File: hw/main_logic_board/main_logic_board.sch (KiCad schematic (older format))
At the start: 3 parts, among them U1 PocketBeagle, U2 BME280, U3 MPU-9250

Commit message: Progress on MLB design
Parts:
- removed U2: BME280, Package_LGA:Bosch_LGA-8_2.5x2.5mm_P0.65mm_ClockwisePinNumbering, symbol Sensor:BME280
- removed U3: MPU-9250, Sensor_Motion:InvenSense_QFN-24_3x3mm_P0.4mm, symbol Sensor_Motion:MPU-9250
- added C1: 47uF, symbol Device:C_Small
- added TP1: TP_5V, TestPoint:TestPoint_Pad_D2.0mm, symbol Connector:TestPoint
- added TP2: TP_3V3, TestPoint:TestPoint_Pad_D2.0mm, symbol Connector:TestPoint
- added TP3: TP_VOUT, TestPoint:TestPoint_Pad_D2.0mm, symbol Connector:TestPoint
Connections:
- net labels added: +3V3, +5V, AIN_1V8, AIN_3V3, GND, GPIO20, GPIO23, GPIO26, GPIO27, I2C_SCL, I2C_SDA, PWM0, PWM1, RC_OUT_2, RC_OUT_3, RC_OUT_4, RC_OUT_5, RC_OUT_6, SPI1_CLK, SPI1_CS0, SPI1_CS1, SPI1_MISO, SPI1_MOSI, SPI1_SCLK, UART0_RX, UART0_TX, UART2_RX, UART2_TX, UART4_RX, UART4_TX
- wire segments 0 -> 53
- no-connect marks 0 -> 25
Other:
- moved on the sheet: U1

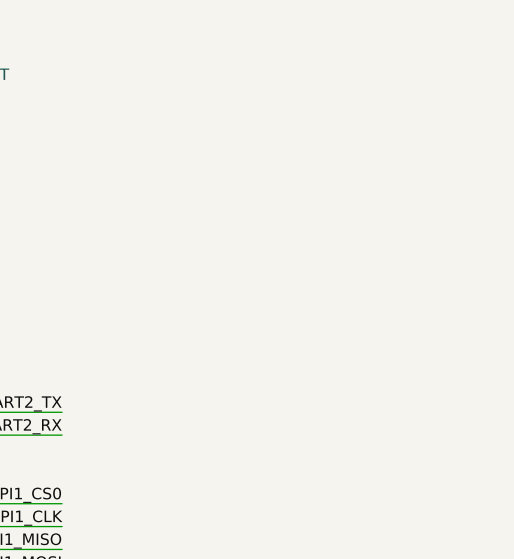
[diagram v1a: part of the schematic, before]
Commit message: Finish initial power schematics, swap some footprints for visualization in pcb view
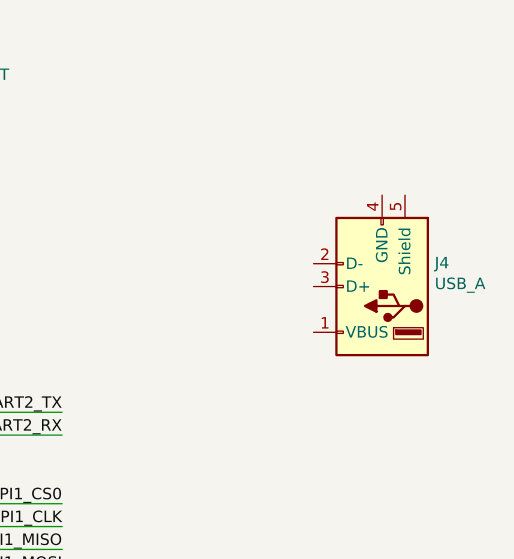
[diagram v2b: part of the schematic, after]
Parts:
- added J4: USB_A, Connector_USB:USB_A_Stewart_SS-52100-001_Horizontal, symbol Connector:USB_A
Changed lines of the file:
@@
 Text Label 5300 4900 0    50   ~ 0
 RC_OUT_6
+$Comp
+L Connector:USB_A J4
+U 1 1 5EAEF3D4
+P 9750 1950
+F 0 "J4" H 9520 1847 50  0000 R CNN
+F 1 "USB_A" H 9520 1938 50  0000 R CNN
+F 2 "Connector_USB:USB_A_Stewart_SS-52100-001_Horizontal" H 9900 1900 50  0001 C CNN
+F 3 " ~" H 9900 1900 50  0001 C CNN
+	1    9750 1950
+	-1   0    0    1
+$EndComp
 $EndSCHEMATC

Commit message: Finish prelim schematic + PCB component placement
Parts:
- added D1, D2, D3, D4: WS2813, LED_SMD:LED_WS2812_PLCC6_5.0x5.0mm_P1.6mm, symbol LED:WS2813
- added H1, H12, H6, H7: GND, MountingHole:MountingHole_2.2mm_M2_Pad_Via, symbol Mechanical:MountingHole_Pad
- added H10, H3, H4, H9: PWR, MountingHole:MountingHole_2.2mm_M2_Pad_Via, symbol Mechanical:MountingHole_Pad
- added H11, H2, H5, H8: SIG, MountingHole:MountingHole_2.2mm_M2_Pad_Via, symbol Mechanical:MountingHole_Pad
- added J10: RC_OUT_6, Connector_PinHeader_1.27mm:PinHeader_1x03_P1.27mm_Vertical, symbol Connector_Generic:Conn_01x03
- added J5: RC_OUT_1, Connector_PinHeader_1.27mm:PinHeader_1x03_P1.27mm_Vertical, symbol Connector_Generic:Conn_01x03
- added J6: RC_OUT_2, Connector_PinHeader_1.27mm:PinHeader_1x03_P1.27mm_Vertical, symbol Connector_Generic:Conn_01x03
- added J7: RC_OUT_3, Connector_PinHeader_1.27mm:PinHeader_1x03_P1.27mm_Vertical, symbol Connector_Generic:Conn_01x03
- added J8: RC_OUT_4, Connector_PinHeader_1.27mm:PinHeader_1x03_P1.27mm_Vertical, symbol Connector_Generic:Conn_01x03
- added J9: RC_OUT_5, Connector_PinHeader_1.27mm:PinHeader_1x03_P1.27mm_Vertical, symbol Connector_Generic:Conn_01x03
- added R5: 0R, Resistor_SMD:R_0805_2012Metric, symbol Device:R_Small_US
- added TP4: AIN_VREF+, TestPoint:TestPoint_Pad_D1.0mm, symbol Connector:TestPoint
- added TP5: AIN_VREF-, TestPoint:TestPoint_Pad_D1.0mm, symbol Connector:TestPoint
- added U9: USBLC6-2P6, lib:SOT50P160X60-6N, symbol USBLC6-2P6:USBLC6-2P6
- C1: footprint (none) -> Capacitor_SMD:C_0805_2012Metric
- TP1: value TP_5V -> TP_5V_VIN; footprint TestPoint:TestPoint_Pad_D2.0mm -> TestPoint:TestPoint_Pad_D1.0mm
- TP2: value TP_3V3 -> TP_3V3_PB; footprint TestPoint:TestPoint_Pad_D2.0mm -> TestPoint:TestPoint_Pad_D1.0mm
- TP3: footprint TestPoint:TestPoint_Pad_D2.0mm -> TestPoint:TestPoint_Pad_D1.0mm
- U1: footprint Module:BeagleBoard_PocketBeagle -> lib:BeagleBoard_PocketBeagle_SMD
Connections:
- net +5V: now also U1.5 (USB1.VBUS), R5.1
- net GND: now also J4.4 (GND), J4.5 (Shield), U1.13 (USB1.ID), H1.1, H12.1, H6.1, H7.1, J10.3 (Pin_3), J5.3 (Pin_3), J6.3 (Pin_3), J7.3 (Pin_3), J8.3 (Pin_3), J9.3 (Pin_3), U9.2 (GND)
- net RC_OUT_2: now also H5.1, J6.2 (Pin_2)
- net RC_OUT_3: now also H8.1, J7.2 (Pin_2)
- net RC_OUT_4: now also H11.1, J8.2 (Pin_2)
- net RC_OUT_5: now also J9.2 (Pin_2)
- net RC_OUT_6: now also J10.2 (Pin_2)
- net at U1.11 (USB1.D+): now also U9.3 (I/O2_1)
- net at U1.17 (AIN.VREF-): now also TP5.1
- net at U1.18 (AIN.VREF+): now also TP4.1
- net AIN_1V8_1: now reaches U1.21 (AIN1(1.8V))
- net RC_OUT_1: now reaches U1.29 (PRU0.7)
- net RC_OUT_1: now also H2.1, J5.2 (Pin_2)
- net I2C1_SCL: now reaches U1.45 (I2C1.SCL)
- net I2C1_SDA: now reaches U1.47 (I2C1.SDA)
- net at U1.9 (USB1.D-): now also U9.1 (I/O1_1)
- net at J4.1 (VBUS): now also R5.2, U9.5 (VBUS)
- net at J4.2 (D-): now also U9.6 (I/O1_2)
- net at J4.3 (D+): now also U9.4 (I/O2_2)
- net +3V3 renamed 3V3_PB
- net AIN_1V8 renamed AIN_1V8_0
- net I2C_SCL renamed I2C2_SCL
- net I2C_SDA renamed I2C2_SDA
- new net +BATT: H10.1, H3.1, H4.1, H9.1, J10.1 (Pin_1), J5.1 (Pin_1), J6.1 (Pin_1), J7.1 (Pin_1), J8.1 (Pin_1), J9.1 (Pin_1)
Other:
- moved on the sheet: J4, TP3

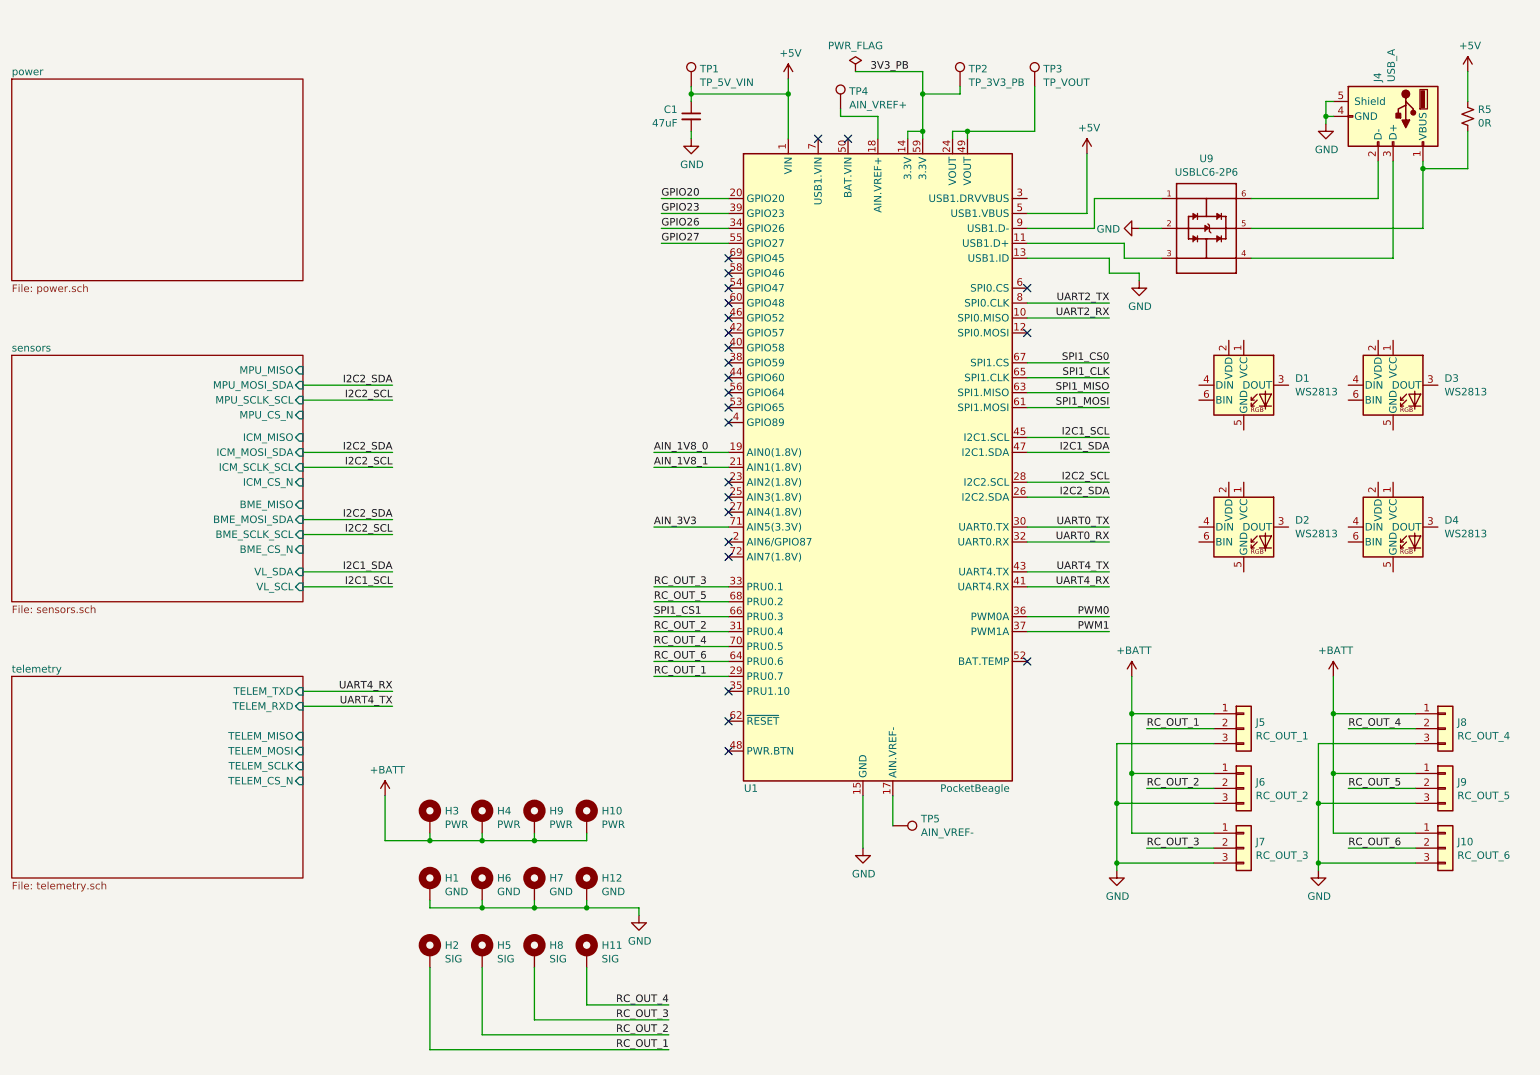
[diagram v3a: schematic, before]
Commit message: Add debug headers, LED wiring, remove MPU
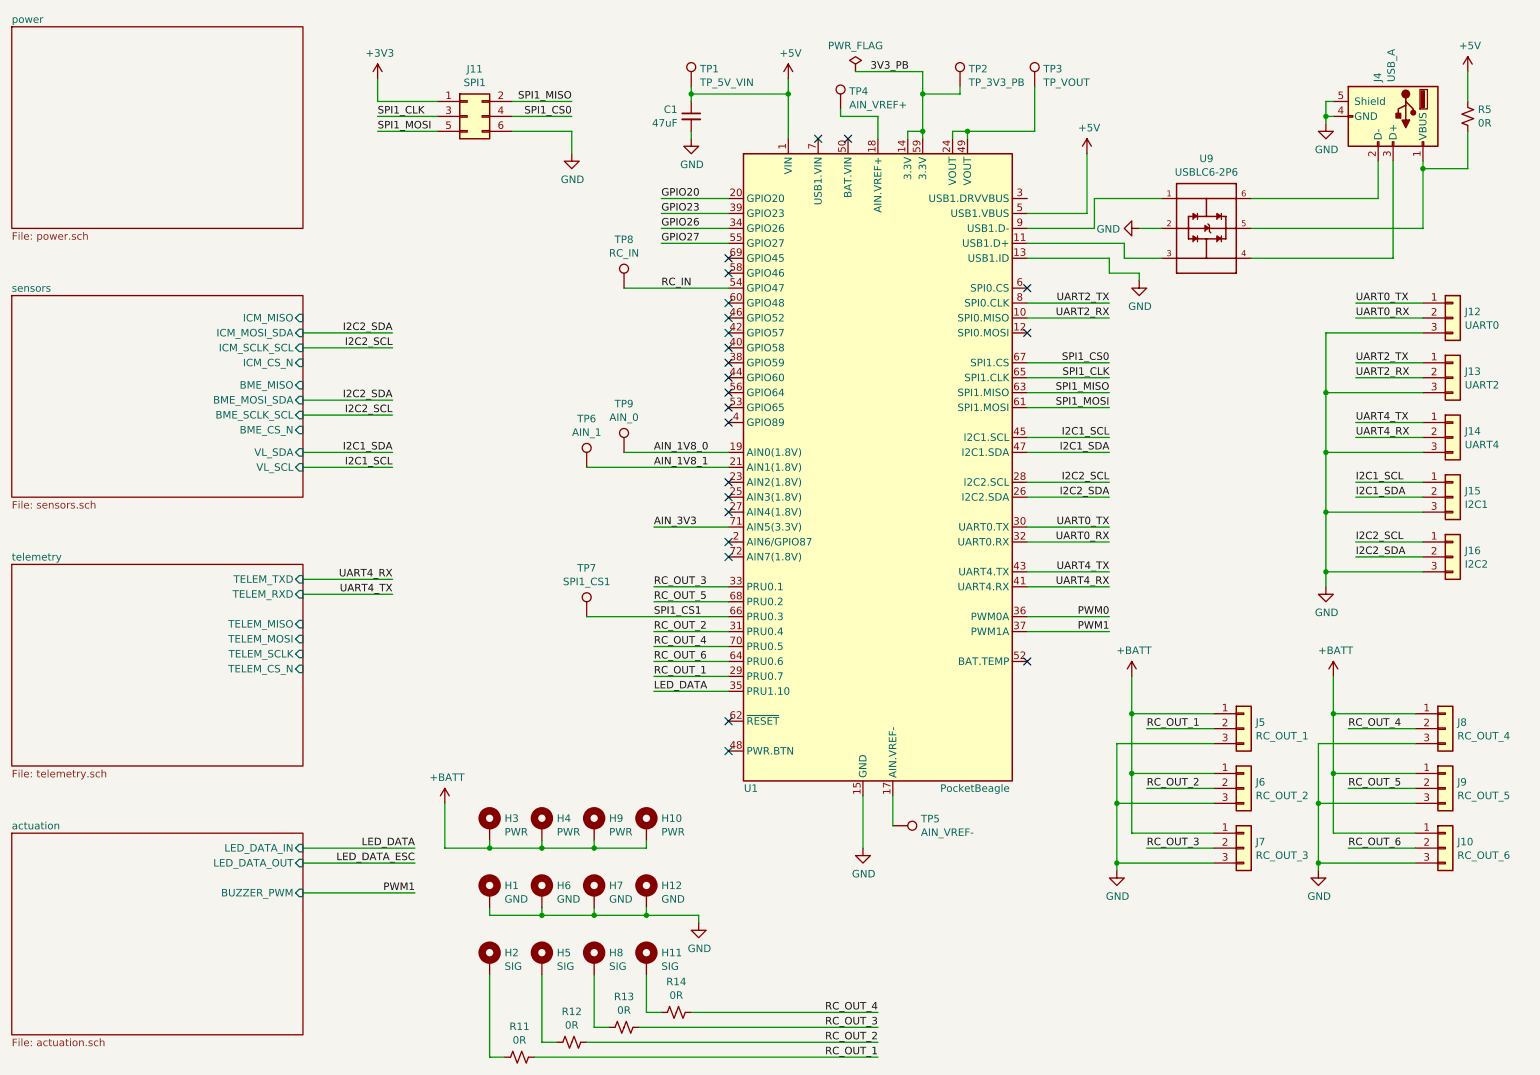
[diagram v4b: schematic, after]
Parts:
- removed D1, D2, D3, D4: WS2813, LED_SMD:LED_WS2812_PLCC6_5.0x5.0mm_P1.6mm, symbol LED:WS2813
- added J11: SPI1, Connector_PinHeader_1.27mm:PinHeader_2x03_P1.27mm_Vertical_SMD, symbol Connector_Generic:Conn_02x03_Odd_Even
- added J12: UART0, Connector_PinHeader_1.27mm:PinHeader_1x03_P1.27mm_Vertical_SMD_Pin1Left, symbol Connector_Generic:Conn_01x03
- added J13: UART2, Connector_PinHeader_1.27mm:PinHeader_1x03_P1.27mm_Vertical_SMD_Pin1Left, symbol Connector_Generic:Conn_01x03
- added J14: UART4, Connector_PinHeader_1.27mm:PinHeader_1x03_P1.27mm_Vertical_SMD_Pin1Left, symbol Connector_Generic:Conn_01x03
- added J15: I2C1, Connector_PinHeader_1.27mm:PinHeader_1x03_P1.27mm_Vertical_SMD_Pin1Left, symbol Connector_Generic:Conn_01x03
- added J16: I2C2, Connector_PinHeader_1.27mm:PinHeader_1x03_P1.27mm_Vertical_SMD_Pin1Left, symbol Connector_Generic:Conn_01x03
- added R11, R12, R13, R14: 0R, Resistor_SMD:R_0805_2012Metric, symbol Device:R_Small_US
- added TP6: AIN_1, TestPoint:TestPoint_Pad_D1.0mm, symbol Connector:TestPoint
- added TP7: SPI1_CS1, TestPoint:TestPoint_Pad_D1.0mm, symbol Connector:TestPoint
- added TP8: RC_IN, TestPoint:TestPoint_Pad_D1.0mm, symbol Connector:TestPoint
- added TP9: AIN_0, TestPoint:TestPoint_Pad_D1.0mm, symbol Connector:TestPoint
- J10, J5, J6, J7, J8, J9: footprint Connector_PinHeader_1.27mm:PinHeader_1x03_P1.27mm_Vertical -> Connector_PinHeader_2.54mm:PinHeader_1x03_P2.54mm_Vertical
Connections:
- net AIN_1V8_0: now also TP9.1
- net AIN_1V8_1: now also TP6.1
- net GND: now also J11.6 (Pin_6), J12.3 (Pin_3), J13.3 (Pin_3), J14.3 (Pin_3), J15.3 (Pin_3), J16.3 (Pin_3)
- net I2C1_SCL: now also J15.1 (Pin_1)
- net I2C1_SDA: now also J15.2 (Pin_2)
- net I2C2_SCL: now also J16.1 (Pin_1)
- net I2C2_SDA: now also J16.2 (Pin_2)
- net RC_OUT_1: now also R11.2; no longer H2.1
- net RC_OUT_2: now also R12.2; no longer H5.1
- net RC_OUT_3: now also R13.2; no longer H8.1
- net RC_OUT_4: now also R14.2; no longer H11.1
- net SPI1_CLK: now also J11.3 (Pin_3)
- net SPI1_CS0: now also J11.4 (Pin_4)
- net SPI1_CS1: now also TP7.1
- net SPI1_MISO: now also J11.2 (Pin_2)
- net SPI1_MOSI: now also J11.5 (Pin_5)
- net UART0_RX: now also J12.2 (Pin_2)
- net UART0_TX: now also J12.1 (Pin_1)
- net UART2_RX: now also J13.2 (Pin_2)
- net UART2_TX: now also J13.1 (Pin_1)
- net UART4_RX: now also J14.2 (Pin_2)
- net UART4_TX: now also J14.1 (Pin_1)
- net LED_DATA: now reaches U1.35 (PRU1.10)
- net RC_IN: now reaches U1.54 (GPIO47)
- net RC_IN: now also TP8.1
- new net: H2.1, R11.1
- new net: H5.1, R12.1
- new net: H8.1, R13.1
- new net: H11.1, R14.1
- new net +3V3: J11.1 (Pin_1)
- no-connect marks 25 -> 23
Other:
- moved on the sheet: H1, H10, H11, H12, H2, H3, H4, H5, H6, H7, H8, H9

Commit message: Add 3D model files, lay out switching circuit, other tweaks
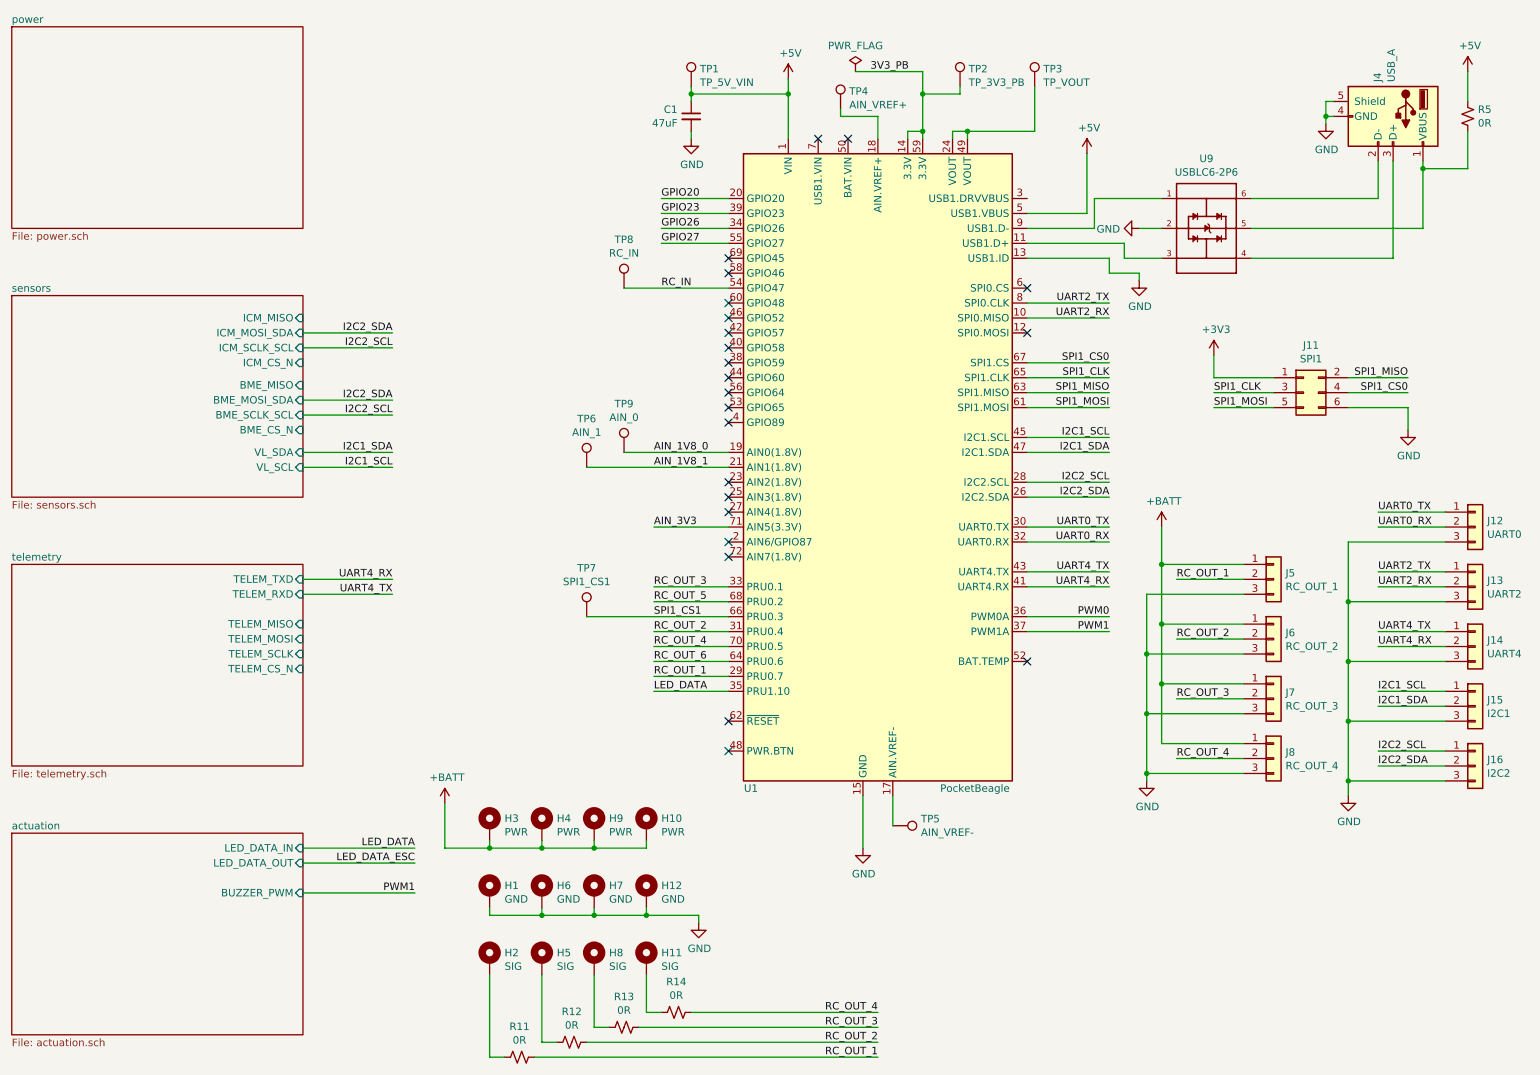
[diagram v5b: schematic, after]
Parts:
- removed J10: RC_OUT_6, Connector_PinHeader_2.54mm:PinHeader_1x03_P2.54mm_Vertical, symbol Connector_Generic:Conn_01x03
- removed J9: RC_OUT_5, Connector_PinHeader_2.54mm:PinHeader_1x03_P2.54mm_Vertical, symbol Connector_Generic:Conn_01x03
- J12, J13, J14, J15, J16: footprint Connector_PinHeader_1.27mm:PinHeader_1x03_P1.27mm_Vertical_SMD_Pin1Left -> Connector_PinHeader_1.27mm:PinHeader_1x03_P1.27mm_Vertical
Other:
- moved on the sheet: J11, J12, J13, J14, J15, J16, J5, J6, J7, J8

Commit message: Add power + GPIO LEDs
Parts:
- added D6, D7, D8: LED, Diode_SMD:D_0805_2012Metric, symbol Device:LED
- added R15, R16, R17: 1K, Resistor_SMD:R_0805_2012Metric, symbol Device:R_Small_US
- added R20: 20K, Resistor_SMD:R_0805_2012Metric, symbol Device:R_Small_US
- added R21: 7K5, Resistor_SMD:R_0805_2012Metric, symbol Device:R_Small_US
- added TP10: USB_VIN, TestPoint:TestPoint_Pad_D1.0mm, symbol Connector:TestPoint
- TP5: value AIN_VREF- -> GPIO27
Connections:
- net +BATT: now also R20.1
- net AIN_3V3: now also R20.2, R21.1
- net GND: now also U1.17 (AIN.VREF-), D6.1 (K), D7.1 (K), D8.1 (K), R21.2
- net GPIO20: now also R15.1
- net GPIO23: now also R16.1
- net GPIO26: now also R17.1
- net GPIO27: now also TP5.1
- net at TP3.1, U1.49 (VOUT): no longer U1.24 (VOUT)
- net at U1.7 (USB1.VIN): now also TP10.1
- new net: D8.2 (A), R17.2
- new net: D7.2 (A), R16.2
- new net: D6.2 (A), R15.2
- no-connect marks 23 -> 24
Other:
- moved on the sheet: TP4, TP8

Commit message: Add current sensor, layout progress, and remove temp mech files
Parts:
- removed R20: 20K, Resistor_SMD:R_0805_2012Metric, symbol Device:R_Small_US
- removed R21: 7K5, Resistor_SMD:R_0805_2012Metric, symbol Device:R_Small_US
- removed TP9: AIN_0, TestPoint:TestPoint_Pad_D1.0mm, symbol Connector:TestPoint
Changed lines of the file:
@@
 F0 "power" 50
 F1 "power.sch" 50
+F2 "BATTC_3V3" I R 2950 750 50
+F3 "BATTV_1V8" I R 2950 850 50
 $EndSheet
 $Comp
@@
 $EndComp
 $Comp
-L Connector:TestPoint TP9
-U 1 1 5ECC7984
-P 5100 3500
-F 0 "TP9" H 5100 3825 50  0000 C CNN
-F 1 "AIN_0" H 5100 3734 50  0000 C CNN
-F 2 "TestPoint:TestPoint_Pad_D1.0mm" H 5300 3500 50  0001 C CNN
-F 3 "~" H 5300 3500 50  0001 C CNN
-	1    5100 3500
-	1    0    0    -1
-$EndComp
-$Comp
 L Connector:TestPoint TP6
 U 1 1 5ECD0003
@@
 	1    0    0    -1
 $EndComp
-Wire Wire Line
-	5100 3500 5800 3500
 Wire Wire Line
 	4850 3600 5800 3600
@@
 Wire Wire Line
 	5200 850  5200 1800
-$Comp
-L power:+BATT #PWR0156
-U 1 1 5EE55BF0
-P 4200 3650
-F 0 "#PWR0156" H 4200 3500 50  0001 C CNN
-F 1 "+BATT" H 4215 3823 50  0000 C CNN
-F 2 "" H 4200 3650 50  0001 C CNN
-F 3 "" H 4200 3650 50  0001 C CNN
-	1    4200 3650
-	1    0    0    -1
-$EndComp
-$Comp
-L Device:R_Small_US R20
-U 1 1 5EE56C28
-P 4200 3850
-F 0 "R20" H 4268 3896 50  0000 L CNN
-F 1 "20K" H 4268 3805 50  0000 L CNN
-F 2 "Resistor_SMD:R_0805_2012Metric" H 4200 3850 50  0001 C CNN
-F 3 "~" H 4200 3850 50  0001 C CNN
-	1    4200 3850
-	1    0    0    -1
-$EndComp
-$Comp
-L Device:R_Small_US R21
-U 1 1 5EE62704
-P 4200 4150
-F 0 "R21" H 4268 4196 50  0000 L CNN
-F 1 "7K5" H 4268 4105 50  0000 L CNN
-F 2 "Resistor_SMD:R_0805_2012Metric" H 4200 4150 50  0001 C CNN
-F 3 "~" H 4200 4150 50  0001 C CNN
-	1    4200 4150
-	1    0    0    -1
-$EndComp
-$Comp
-L power:GND #PWR0157
-U 1 1 5EE6E521
-P 4200 4350
-F 0 "#PWR0157" H 4200 4100 50  0001 C CNN
-F 1 "GND" H 4205 4177 50  0000 C CNN
-F 2 "" H 4200 4350 50  0001 C CNN
-F 3 "" H 4200 4350 50  0001 C CNN
-	1    4200 4350
-	1    0    0    -1
-$EndComp
-Wire Wire Line
-	4200 4350 4200 4250
-Wire Wire Line
-	4200 4050 4200 4000
-Wire Wire Line
-	4200 3750 4200 3650
-Wire Wire Line
-	4200 4000 5800 4000
-Connection ~ 4200 4000
-Wire Wire Line
-	4200 4000 4200 3950
 NoConn ~ 7300 1400
+Wire Wire Line
+	5300 4000 5800 4000
+Wire Wire Line
+	2950 750  3500 750
+Wire Wire Line
+	2950 850  3500 850
+Wire Wire Line
+	5800 3500 5300 3500
+Text Label 3500 850  2    50   ~ 0
+AIN_1V8_0
+Text Label 3500 750  2    50   ~ 0
+AIN_3V3
 $EndSCHEMATC
